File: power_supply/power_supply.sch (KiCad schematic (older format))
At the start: 34 parts

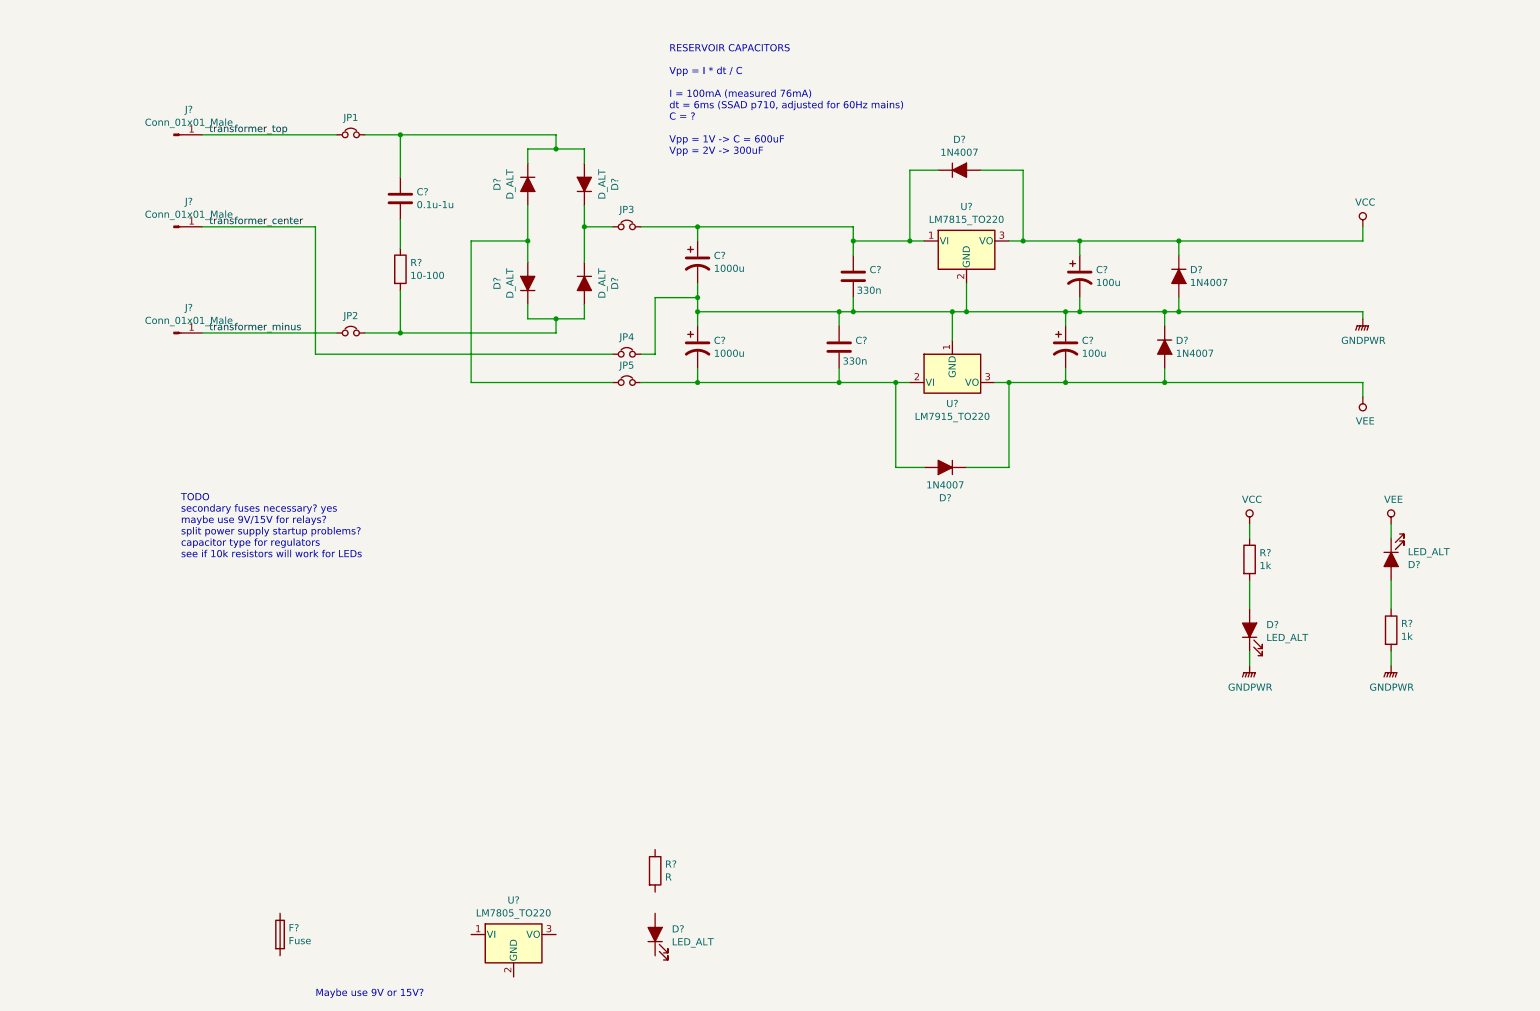
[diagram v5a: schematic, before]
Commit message: add many component details & footprints to power supply
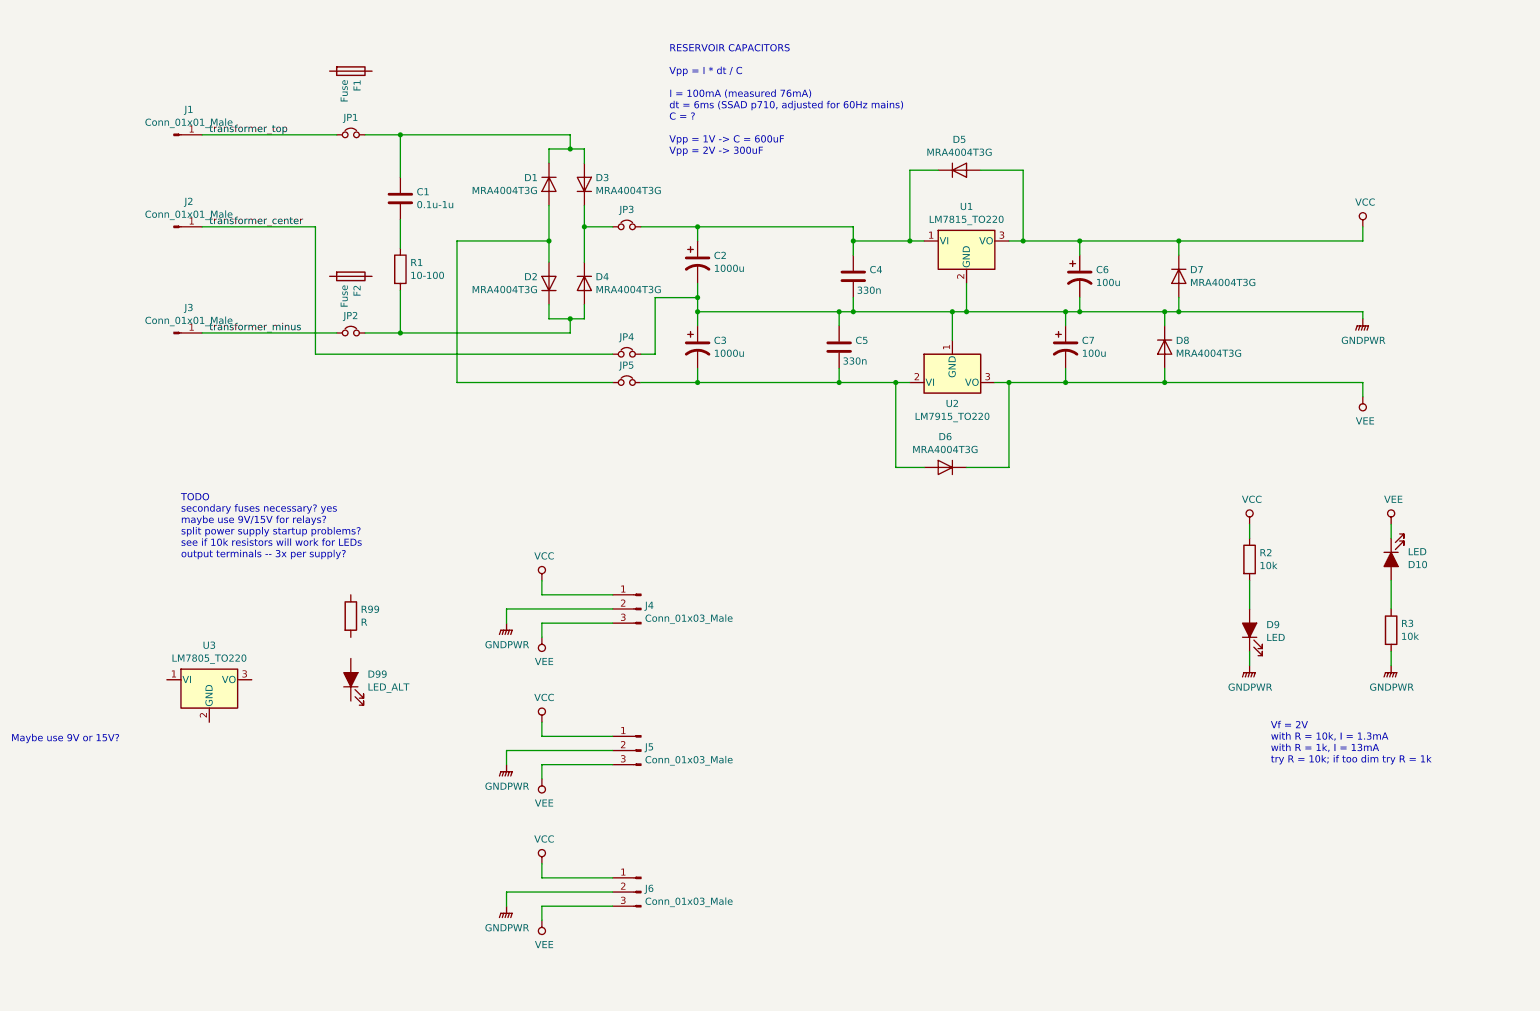
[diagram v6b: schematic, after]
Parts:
- removed C?: 100u, symbol Device:CP1
- removed C?: 1000u, symbol Device:CP1
- removed C?: 330n, symbol Device:C
- removed D? (x4): 1N4007, symbol Device:D_ALT
- removed D? (x4): D_ALT, symbol Device:D_ALT
- removed D?: LED_ALT, symbol Device:LED_ALT
- removed F?: Fuse, symbol Device:Fuse
- added C3: 1000u, Capacitor_THT:CP_Radial_D12.5mm_P5.00mm, symbol Device:CP1
- added C5: 330n, Capacitor_SMD:C_0805_2012Metric_Pad1.15x1.40mm_HandSolder, symbol Device:C
- added C7: 100u, Capacitor_THT:CP_Radial_D6.3mm_P2.50mm, symbol Device:CP1
- added D1, D2, D3, D4, D5, D6, D7, D8: MRA4004T3G, Diode_SMD:D_SMA, symbol Diode:MRA4004T3G
- added D10: LED, LED_SMD:LED_0603_1608Metric, symbol Device:LED_ALT
- added F1, F2: Fuse, Fuse:Fuseholder_Cylinder-5x20mm_Schurter_0031_8201_Horizontal_Open, symbol Device:Fuse
- added J4, J5, J6: Conn_01x03_Male, Connector_Molex_SL:Molex_SL_A-70543-0002_1x03_P2.54mm_Vertical, symbol Connector:Conn_01x03_Male
- C2: renamed from C?; footprint (none) -> Capacitor_THT:CP_Radial_D12.5mm_P5.00mm; Distributor (none) -> Digikey; Distributor PN (none) -> 493-1111-ND; Manufacturer (none) -> Nichicon; Manufacturer PN (none) -> UVR1H102MHD; URL (none) -> https://www.digikey.com/product-detail/en/nichicon/UVR1H102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; Unit Price (none) -> 0.86
- C4: renamed from C?; footprint (none) -> Capacitor_SMD:C_0805_2012Metric_Pad1.15x1.40mm_HandSolder; Distributor (none) -> Digikey; Distributor PN (none) -> 1276-1123-1-ND; Manufacturer (none) -> Samsung; Manufacturer PN (none) -> CL21B334KBFNNNE; URL (none) -> https://www.digikey.com/product-detail/en/samsung-electro-m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; Unit Price (none) -> 0.19
- C6: renamed from C?; footprint (none) -> Capacitor_THT:CP_Radial_D6.3mm_P2.50mm; Distributor (none) -> Digikey; Distributor PN (none) -> 493-1081-ND; Manufacturer (none) -> Nichicon; Manufacturer PN (none) -> UVR1V101MED; URL (none) -> https://www.digikey.com/product-detail/en/nichicon/UVR1V101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; Unit Price (none) -> 0.25
- D9: renamed from D?; value LED_ALT -> LED; footprint (none) -> LED_SMD:LED_0603_1608Metric; Distributor (none) -> Digikey; Distributor PN (none) -> 160-1447-1-ND; Manufacturer (none) -> Lite-On; Manufacturer PN (none) -> LTST-C191KRKT; URL (none) -> https://www.digikey.com/product-detail/en/lite-on-inc/LTST-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; Unit Price (none) -> 0.29
- D99: renamed from D?; footprint (none) -> LED_SMD:LED_0603_1608Metric_Pad1.05x0.95mm_HandSolder
- JP1, JP2, JP3, JP4, JP5: footprint (none) -> Connector_PinHeader_2.54mm:PinHeader_1x02_P2.54mm_Vertical
- R2, R3: renamed from R?; value 1k -> 10k; footprint (none) -> Resistor_SMD:R_0603_1608Metric_Pad1.05x0.95mm_HandSolder
- R99: renamed from R?; footprint (none) -> Resistor_SMD:R_0603_1608Metric_Pad1.05x0.95mm_HandSolder
- gave numbers to parts that had none: 8
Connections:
- net GNDPWR: now also C3.1, C5.1, C7.1, D7.2 (A), D8.1 (K), J4.2 (Pin_2), J5.2 (Pin_2), J6.2 (Pin_2)
- net VCC: now also D5.2 (A), D7.1 (K), J4.1 (Pin_1), J5.1 (Pin_1), J6.1 (Pin_1)
- net VEE: now also C7.2, D10.1 (K), D6.1 (K), D8.2 (A), J4.3 (Pin_3), J5.3 (Pin_3), J6.3 (Pin_3)
- net at C2.1, C4.1, JP3.2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: now also D5.1 (K)
- net at JP5.2, U2.2 (VI): now also C3.2, C5.2, D6.2 (A)
- net at C1.1, JP1.2: now also D1.1 (K), D3.2 (A)
- net at JP5.1: now also D1.2 (A), D2.2 (A)
- net at JP3.1: now also D3.1 (K), D4.1 (K)
- net at JP2.2, R1.2: now also D2.1 (K), D4.2 (A)
- net at R3.1: now also D10.2 (A)
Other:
- note added: "TODO\nsecondary fuses necessary? yes\nmaybe use 9V/15V for relays?\nsplit power supply startup problems?\nsee if 10k resistors will work for LEDs\noutput terminals -- 3x per supply?"
- note added: "Vf = 2V\nwith R = 10k, I = 1.3mA\nwith R = 1k, I = 13mA\ntry R = 10k; if too dim try R = 1k"
- note removed: "TODO\nsecondary fuses necessary? yes\nmaybe use 9V/15V for relays?\nsplit power supply startup problems?\ncapacitor type for regulators\nsee if 10k resistors will work for LEDs"
- moved on the sheet: D99, R99, U3

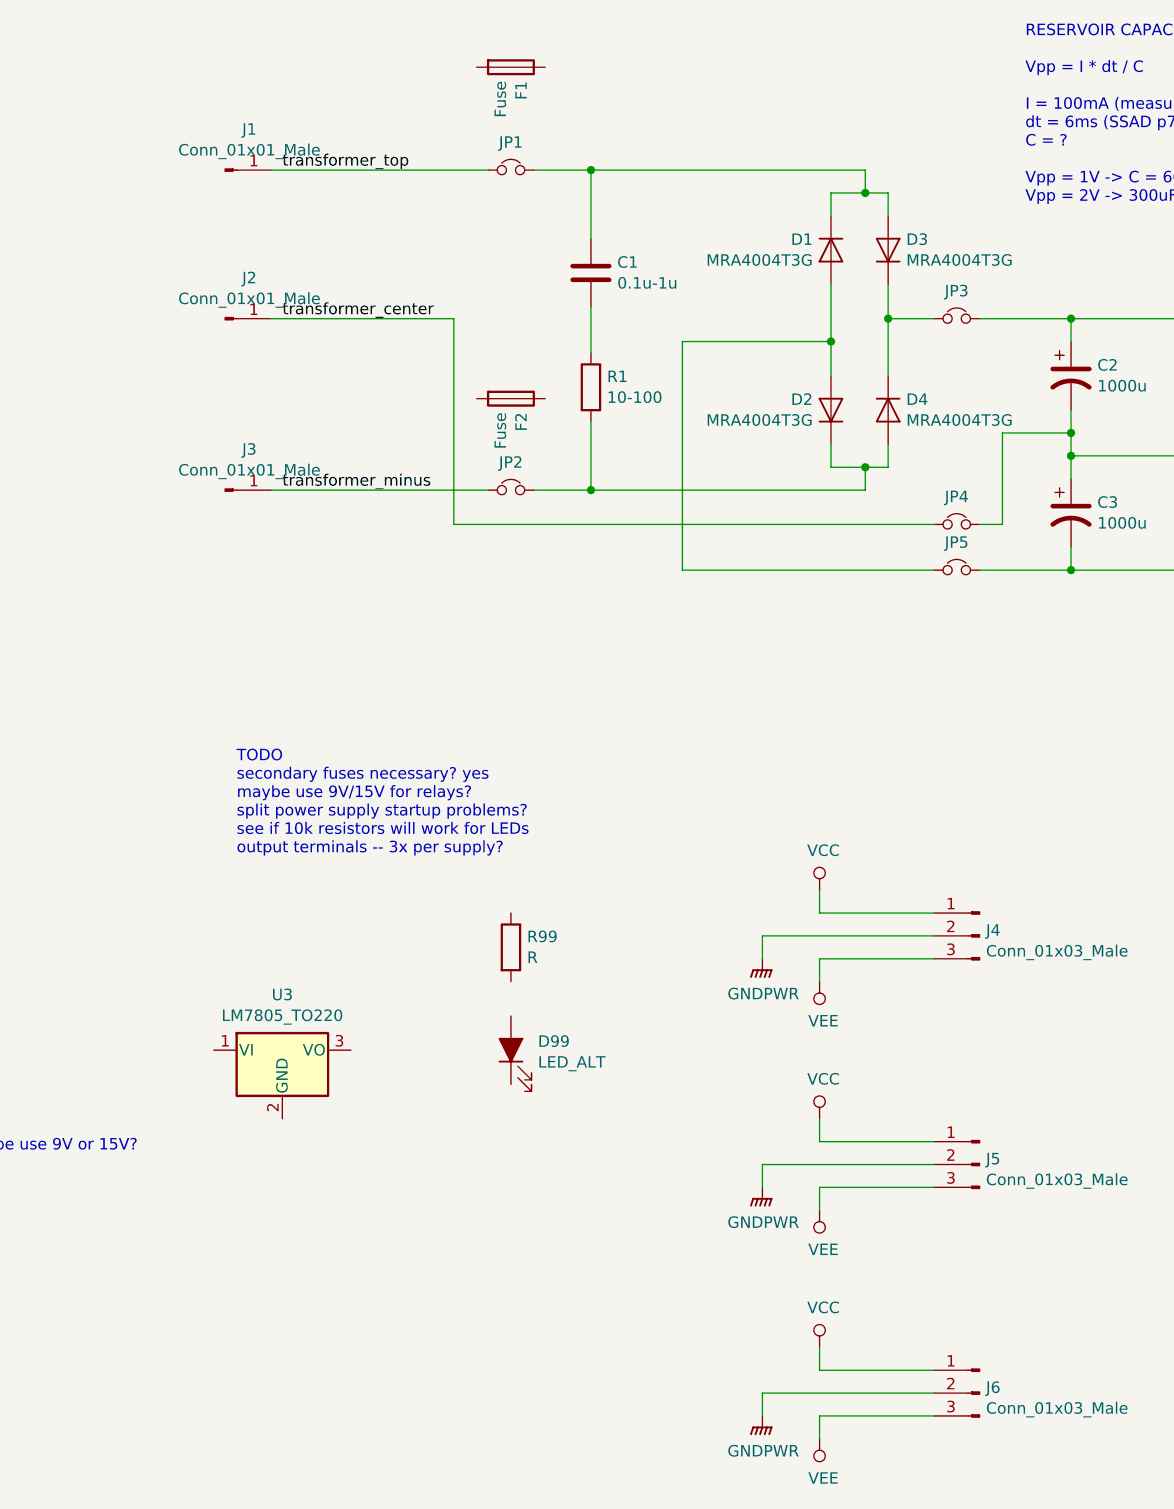
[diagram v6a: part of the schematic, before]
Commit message: change input connector to 1x4 Molex SL
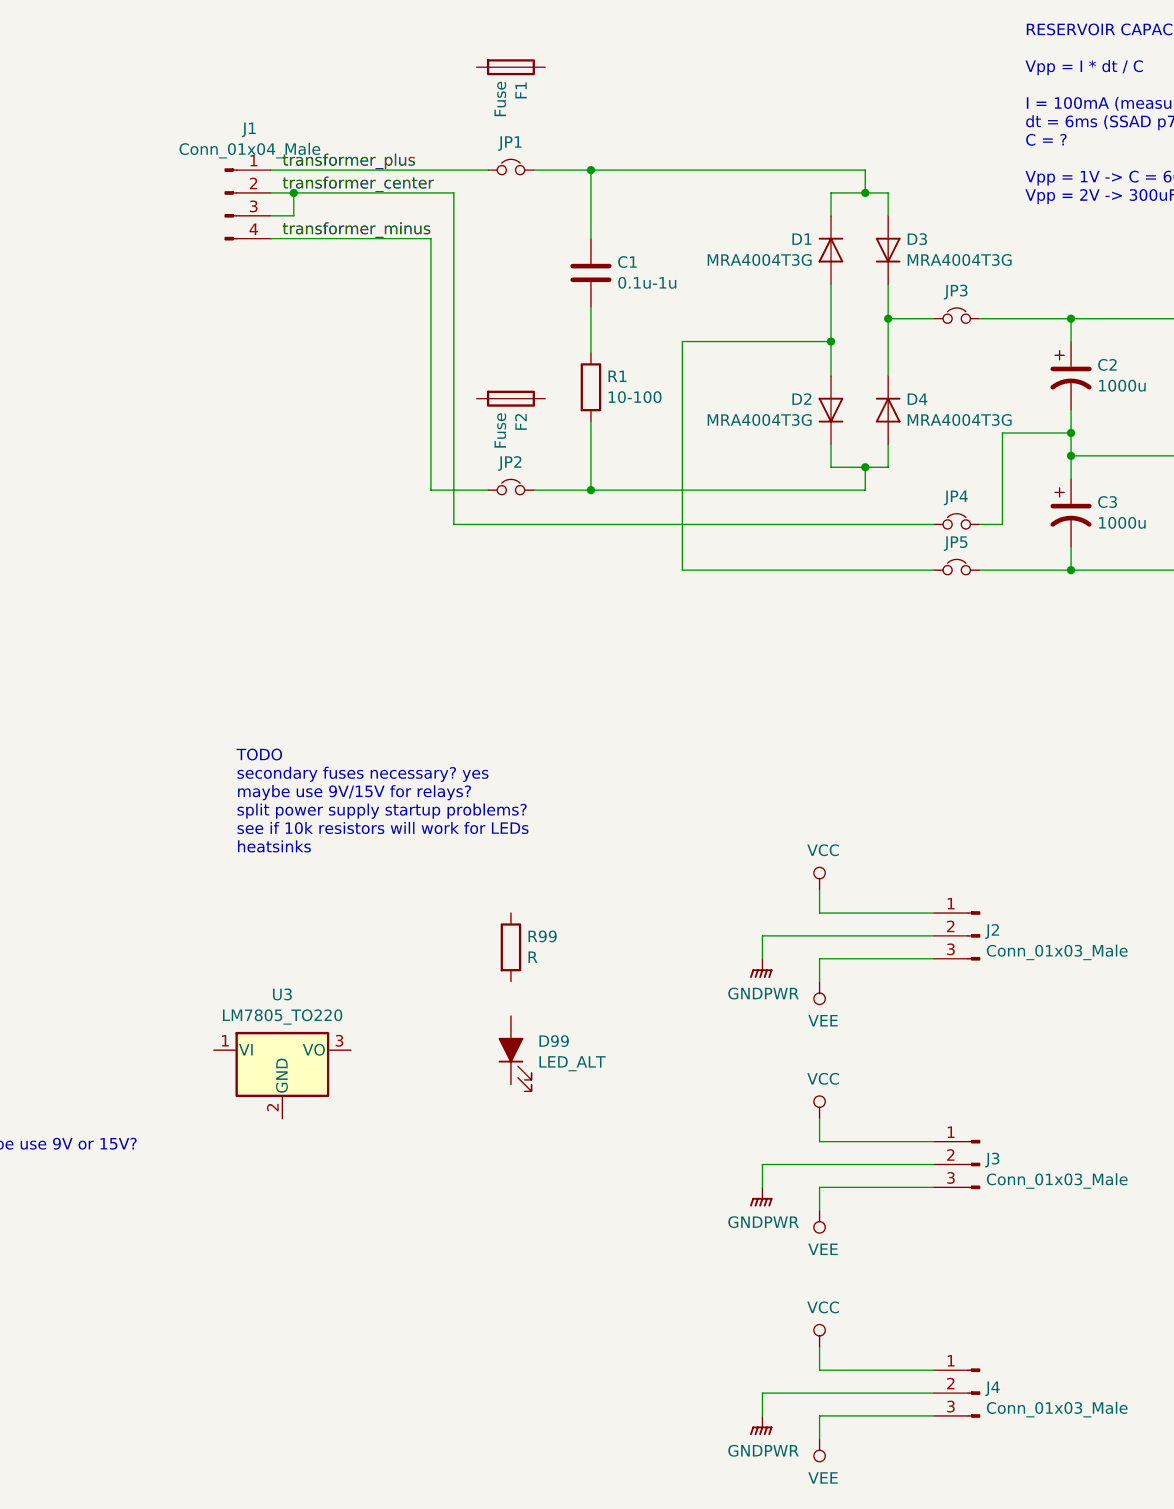
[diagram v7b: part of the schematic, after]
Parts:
- removed J1, J2, J3: Conn_01x01_Male, symbol Connector:Conn_01x01_Male
- added J1: Conn_01x04_Male, Connector_Molex_SL:Molex_SL_A-70543-0003_1x04_P2.54mm_Vertical, symbol Connector:Conn_01x04_Male
- renumbered J4 to J2, J5 to J3, J6 to J4
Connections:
- net transformer_center: now also J1.2 (Pin_2), J1.3 (Pin_3)
- net transformer_minus: now also J1.4 (Pin_4)
- net transformer_top renamed transformer_plus
- net transformer_plus: now also J1.1 (Pin_1)
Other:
- note added: "TODO\nsecondary fuses necessary? yes\nmaybe use 9V/15V for relays?\nsplit power supply startup problems?\nsee if 10k resistors will work for LEDs\nheatsinks"
- note removed: "TODO\nsecondary fuses necessary? yes\nmaybe use 9V/15V for relays?\nsplit power supply startup problems?\nsee if 10k resistors will work for LEDs\noutput terminals -- 3x per supply?"
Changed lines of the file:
@@
 Maybe use 9V or 15V?
 Text Notes 950  4250 0    50   ~ 0
-TODO\nsecondary fuses necessary? yes\nmaybe use 9V/15V for relays?\nsplit power supply startup problems?\nsee if 10k resistors will work for LEDs\noutput terminals -- 3x per supply?
+TODO\nsecondary fuses necessary? yes\nmaybe use 9V/15V for relays?\nsplit power supply startup problems?\nsee if 10k resistors will work for LEDs\nheatsinks
 $Comp
 L Device:R R2
@@
 Wire Wire Line
 	4600 2400 4600 2500
-$Comp
-L Connector:Conn_01x01_Male J1
-U 1 1 5C5CB74D
-P 900 1250
-F 0 "J1" H 1006 1428 50  0000 C CNN
-F 1 "Conn_01x01_Male" H 1006 1337 50  0000 C CNN
-F 2 "" H 900 1250 50  0001 C CNN
-F 3 "~" H 900 1250 50  0001 C CNN
-	1    900  1250
-	1    0    0    -1
-$EndComp
-$Comp
-L Connector:Conn_01x01_Male J3
-U 1 1 5C5CB807
-P 900 2650
-F 0 "J3" H 1006 2828 50  0000 C CNN
-F 1 "Conn_01x01_Male" H 1006 2737 50  0000 C CNN
-F 2 "" H 900 2650 50  0001 C CNN
-F 3 "~" H 900 2650 50  0001 C CNN
-	1    900  2650
-	1    0    0    -1
-$EndComp
-$Comp
-L Connector:Conn_01x01_Male J2
-U 1 1 5C5CB865
-P 900 1900
-F 0 "J2" H 1006 2078 50  0000 C CNN
-F 1 "Conn_01x01_Male" H 1006 1987 50  0000 C CNN
-F 2 "" H 900 1900 50  0001 C CNN
-F 3 "~" H 900 1900 50  0001 C CNN
-	1    900  1900
-	1    0    0    -1
-$EndComp
-Text Label 1150 1900 0    50   ~ 0
+Text Label 1150 1350 0    50   ~ 0
 transformer_center
 Wire Wire Line
-	1100 1900 1900 1900
-Wire Wire Line
-	1900 1900 1900 2800
-Text Label 1150 2650 0    50   ~ 0
+	1100 1350 1200 1350
+Wire Wire Line
+	1900 1350 1900 2800
+Text Label 1150 1550 0    50   ~ 0
 transformer_minus
 Text Label 1150 1250 0    50   ~ 0
-transformer_top
+transformer_plus
 Wire Wire Line
 	4600 3000 5600 3000
@@
 	1    0    0    -1
 $EndComp
-Wire Wire Line
-	1100 2650 2050 2650
 Wire Wire Line
 	2250 2650 2500 2650
@@
 $EndComp
 $Comp
-L Connector:Conn_01x03_Male J4
+L Connector:Conn_01x03_Male J2
 U 1 1 5CA83316
 P 4200 4600
-F 0 "J4" H 4172 4624 50  0000 R CNN
+F 0 "J2" H 4172 4624 50  0000 R CNN
 F 1 "Conn_01x03_Male" H 4172 4533 50  0000 R CNN
 F 2 "Connector_Molex_SL:Molex_SL_A-70543-0002_1x03_P2.54mm_Vertical" H 4200 4600 50  0001 C CNN
@@
 $EndComp
 $Comp
-L Connector:Conn_01x03_Male J5
+L Connector:Conn_01x03_Male J3
 U 1 1 5CA83A0D
 P 4200 5600
-F 0 "J5" H 4172 5624 50  0000 R CNN
+F 0 "J3" H 4172 5624 50  0000 R CNN
 F 1 "Conn_01x03_Male" H 4172 5533 50  0000 R CNN
 F 2 "Connector_Molex_SL:Molex_SL_A-70543-0002_1x03_P2.54mm_Vertical" H 4200 5600 50  0001 C CNN
@@
 $EndComp
 $Comp
-L Connector:Conn_01x03_Male J6
+L Connector:Conn_01x03_Male J4
 U 1 1 5CA83D7D
 P 4200 6600
-F 0 "J6" H 4172 6624 50  0000 R CNN
+F 0 "J4" H 4172 6624 50  0000 R CNN
 F 1 "Conn_01x03_Male" H 4172 6533 50  0000 R CNN
 F 2 "Connector_Molex_SL:Molex_SL_A-70543-0002_1x03_P2.54mm_Vertical" H 4200 6600 50  0001 C CNN
@@
 Wire Wire Line
 	3250 4600 4000 4600
+Wire Wire Line
+	1100 1550 1800 1550
+Wire Wire Line
+	1800 1550 1800 2650
+Wire Wire Line
+	1800 2650 2050 2650
+$Comp
+L Connector:Conn_01x04_Male J1
+U 1 1 5CAF6792
+P 900 1350
+F 0 "J1" H 1008 1631 50  0000 C CNN
+F 1 "Conn_01x04_Male" H 1008 1540 50  0000 C CNN
+F 2 "Connector_Molex_SL:Molex_SL_A-70543-0003_1x04_P2.54mm_Vertical" H 900 1350 50  0001 C CNN
+F 3 "~" H 900 1350 50  0001 C CNN
+	1    900  1350
+	1    0    0    -1
+$EndComp
+Wire Wire Line
+	1100 1450 1200 1450
+Wire Wire Line
+	1200 1450 1200 1350
+Connection ~ 1200 1350
+Wire Wire Line
+	1200 1350 1900 1350
 $EndSCHEMATC
